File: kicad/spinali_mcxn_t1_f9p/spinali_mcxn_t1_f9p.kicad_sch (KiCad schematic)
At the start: 0 parts

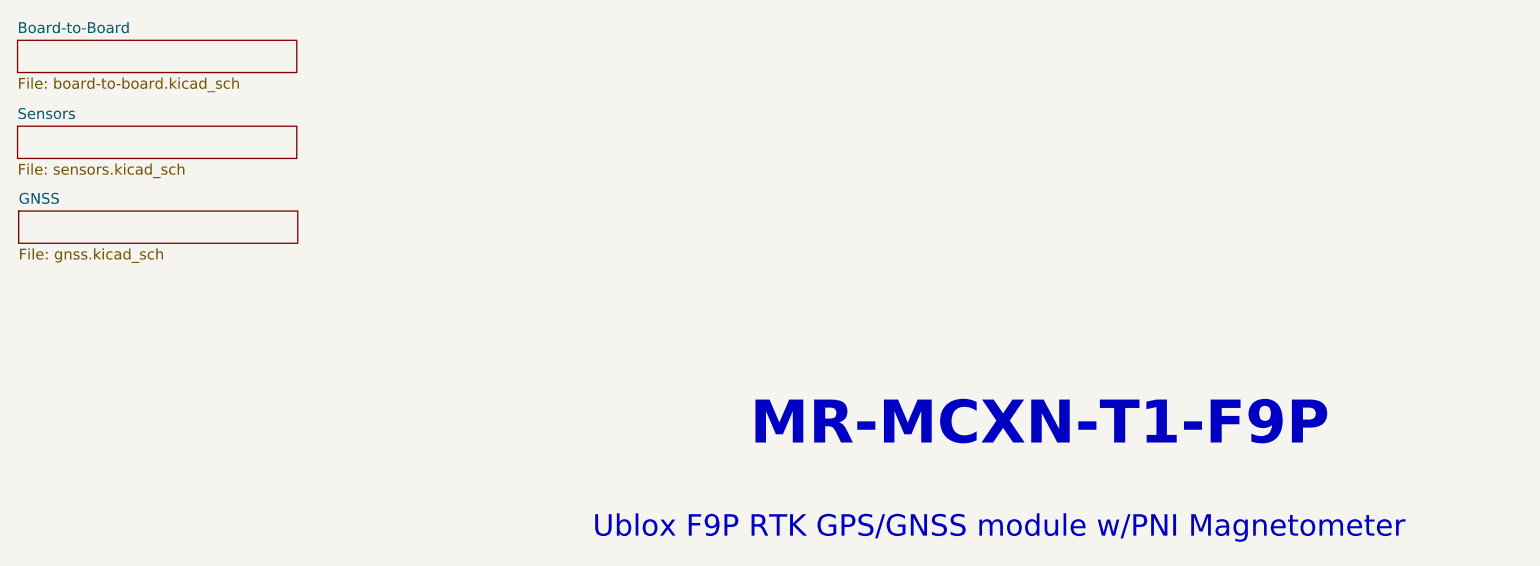
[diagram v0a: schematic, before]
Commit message: Rev A production ready: schematic, layout and BOM fixes
- Rev A production ready.
- Changed 0R pull-up / pull-down resistors where possible to 10k for current protection.
- Fixed R13 footprint to correct package -> 0603 (was 0402).
- Improved BOM headers.
- Added Project text variables so Revision, Title, Designers, etc. is set automatically at multiple places.
- Updated all footprints so they match the library again (previously gave DRC error). Now 3D models also work again.
- Moved Time Pulse LED in layout to make it more visible.
- DRC succesfull.
- Added production folder in .gitignore.

Signed-off-by: Youri Tils <youri.tils@nxp.com>
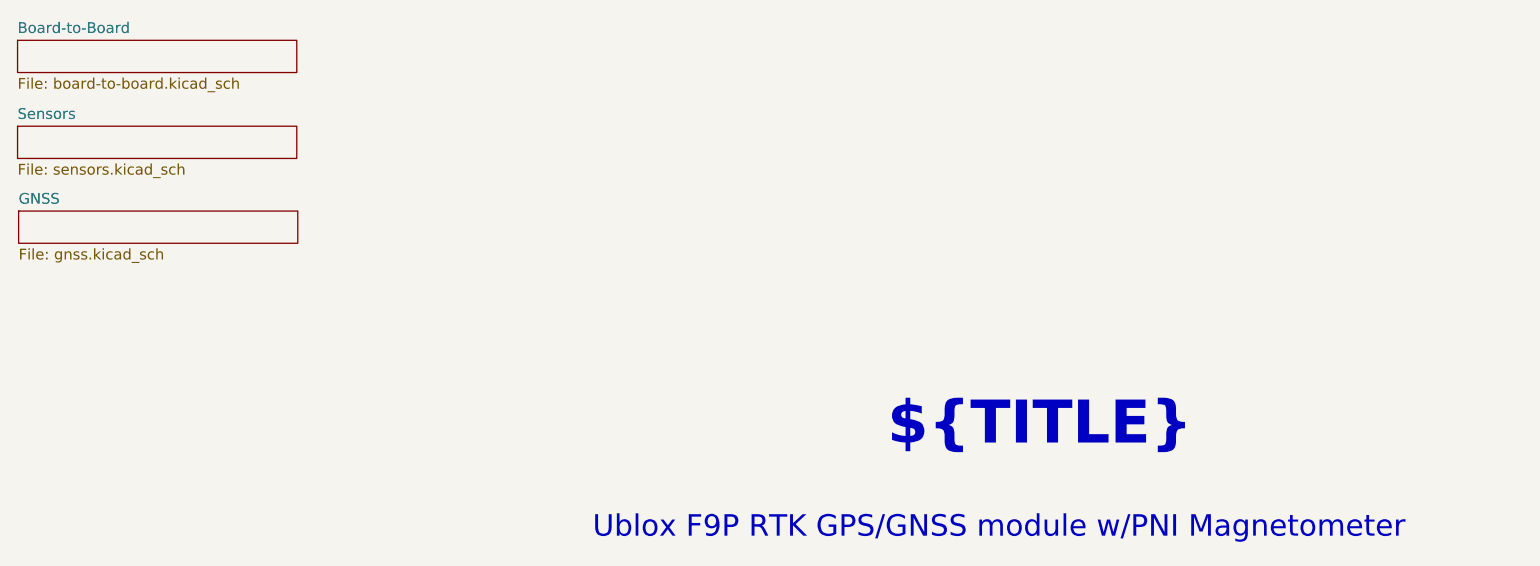
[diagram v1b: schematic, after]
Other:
- company: NXP SEMICONDUCTORS B.V. -> ${COMPANY}
- title: MR-MCXN-T1-F9P -> ${TITLE}
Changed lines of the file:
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@@
 	(paper "A4")
 	(title_block
-		(title "MR-MCXN-T1-F9P")
-		(date "2025-08-27")
-		(rev "A")
-		(company "NXP SEMICONDUCTORS B.V.")
-		(comment 3 "DESIGNER: YOURI TILS, Iain Galloway")
-		(comment 4 "CTO SYSTEM INNOVATIONS / MOBILE ROBOTICS DOMAIN")
+		(title "${TITLE}")
+		(date "2026-08-21")
+		(rev "${BOARD_REV}")
+		(company "${COMPANY}")
+		(comment 1 "DESIGNER: ${DESIGNER}")
+		(comment 2 "${DEPARTMENT}")
+		(comment 3 "REVIEWED BY: ${REVIEWER}")
 	)
 	(text "Ublox F9P RTK GPS/GNSS module w/PNI Magnetometer"
